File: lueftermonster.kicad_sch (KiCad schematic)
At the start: 87 parts, among them J1 Barrel_Jack, J10 Fan, J11 Fan, J12 Fan, J13 Fan, J14 Fan, J15 Fan, J16 Fan, J17 PROG, J2 Fan, J3 Fan, J4 Fan, J5 Fan, J6 Fan, J7 Fan, J8 Fan, J9 Fan, Q1 Q_PMOS_GSD, Q2 Q_NMOS_GSD, Q3 Q_NMOS_GSD, Q4 Q_NMOS_GSD, Q5 Q_NMOS_GSD, U1 ESP32-WROOM-32E, U2 AOZ1280CI, U3 AMS1117-5.0

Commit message: more bom, all the heavy hitters are in now
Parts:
- C11, C12, C13, C14, C15, C16, C17, C18, C19, C20, C21, C22, C23, C24, C25: LCSC (none) -> C215803; MPN (none) -> FH (Guangdong Fenghua Advanced Tech); Manufacturer (none) -> 0805B105K500NT
- J10, J11, J12, J13, J14, J15, J16, J2, J3, J4, J5, J6, J7, J8, J9: LCSC (none) -> C240840; MPN (none) -> 470531000; Manufacturer (none) -> MOLEX
- R3: LCSC (none) -> C25897; MPN (none) -> 0402WGF4992TCE; Manufacturer (none) -> UNI-ROYAL(Uniroyal Elec)
- R4: LCSC (none) -> C26956; MPN (none) -> 0402WGF1582TCE; Manufacturer (none) -> UNI-ROYAL(Uniroyal Elec)
- R6, R7, R8, R9: LCSC (none) -> C25086; MPN (none) -> 0402WGF100KTCE; Manufacturer (none) -> UNI-ROYAL(Uniroyal Elec)

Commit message: snap
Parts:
- added H1, H2, H3, H4: MountingHole_Pad, MountingHole:MountingHole_3.2mm_M3_ISO14580_Pad, symbol Mechanical:MountingHole_Pad
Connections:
- no-connect marks 8 -> 12

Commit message: use 100mil headers for fans
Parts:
- J10, J11, J12, J13, J14, J15, J16, J2, J3, J4, J5, J6, J7, J8, J9: footprint Connector:FanPinHeader_1x04_P2.54mm_Vertical -> Connector_PinHeader_2.54mm:PinHeader_1x04_P2.54mm_Vertical_SMD_Pin1Right; LCSC C240840 -> C780062; MPN 470531000 -> X6511WVS-04H-C60D48R1; Manufacturer MOLEX -> XKB Connection
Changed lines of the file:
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@@
 			)
 		)
-		(property "Footprint" "Connector:FanPinHeader_1x04_P2.54mm_Vertical"
+		(property "Footprint" "Connector_PinHeader_2.54mm:PinHeader_1x04_P2.54mm_Vertical_SMD_Pin1Right"
 			(at 180.34 88.9 0)
 			(effects
@@
 			)
 		)
-		(property "LCSC" "C240840"
+		(property "LCSC" "C780062"
 			(at 180.34 88.9 0)
 			(effects
@@
 			)
 		)
-		(property "MPN" "470531000"
+		(property "MPN" "X6511WVS-04H-C60D48R1"
 			(at 180.34 88.9 0)
 			(effects
@@
 			)
 		)
-		(property "Manufacturer" "MOLEX"
+		(property "Manufacturer" "XKB Connection"
 			(at 180.34 88.9 0)
 			(effects
@@
 			)
 		)
-		(property "Footprint" "Connector:FanPinHeader_1x04_P2.54mm_Vertical"
+		(property "Footprint" "Connector_PinHeader_2.54mm:PinHeader_1x04_P2.54mm_Vertical_SMD_Pin1Right"
 			(at 209.55 88.9 0)
 			(effects
@@
 			)
 		)
-		(property "LCSC" "C240840"
+		(property "LCSC" "C780062"
 			(at 209.55 88.9 0)
 			(effects
@@
 			)
 		)
-		(property "MPN" "470531000"
+		(property "MPN" "X6511WVS-04H-C60D48R1"
 			(at 209.55 88.9 0)
 			(effects
@@
 			)
 		)
-		(property "Manufacturer" "MOLEX"
+		(property "Manufacturer" "XKB Connection"
 			(at 209.55 88.9 0)
 			(effects
@@
 			)
 		)
-		(property "Footprint" "Connector:FanPinHeader_1x04_P2.54mm_Vertical"
+		(property "Footprint" "Connector_PinHeader_2.54mm:PinHeader_1x04_P2.54mm_Vertical_SMD_Pin1Right"
 			(at 267.97 77.47 0)
 			(effects
@@
 			)
 		)
-		(property "LCSC" "C240840"
+		(property "LCSC" "C780062"
 			(at 267.97 77.47 0)
 			(effects
@@
 			)
 		)
-		(property "MPN" "470531000"
+		(property "MPN" "X6511WVS-04H-C60D48R1"
 			(at 267.97 77.47 0)
 			(effects
@@
 			)
 		)
-		(property "Manufacturer" "MOLEX"
+		(property "Manufacturer" "XKB Connection"
 			(at 267.97 77.47 0)
 			(effects
@@
 			)
 		)
-		(property "Footprint" "Connector:FanPinHeader_1x04_P2.54mm_Vertical"
+		(property "Footprint" "Connector_PinHeader_2.54mm:PinHeader_1x04_P2.54mm_Vertical_SMD_Pin1Right"
 			(at 238.76 66.04 0)
 			(effects
@@
 			)
 		)
-		(property "LCSC" "C240840"
+		(property "LCSC" "C780062"
 			(at 238.76 66.04 0)
 			(effects
@@
 			)
 		)
-		(property "MPN" "470531000"
+		(property "MPN" "X6511WVS-04H-C60D48R1"
 			(at 238.76 66.04 0)
 			(effects
@@
 			)
 		)
-		(property "Manufacturer" "MOLEX"
+		(property "Manufacturer" "XKB Connection"
 			(at 238.76 66.04 0)
 			(effects
@@
 			)
 		)
-		(property "Footprint" "Connector:FanPinHeader_1x04_P2.54mm_Vertical"
+		(property "Footprint" "Connector_PinHeader_2.54mm:PinHeader_1x04_P2.54mm_Vertical_SMD_Pin1Right"
 			(at 238.76 77.47 0)
 			(effects
@@
 			)
 		)
-		(property "LCSC" "C240840"
+		(property "LCSC" "C780062"
 			(at 238.76 77.47 0)
 			(effects
@@
 			)
 		)
-		(property "MPN" "470531000"
+		(property "MPN" "X6511WVS-04H-C60D48R1"
 			(at 238.76 77.47 0)
 			(effects
@@
 			)
 		)
-		(property "Manufacturer" "MOLEX"
+		(property "Manufacturer" "XKB Connection"
 			(at 238.76 77.47 0)
 			(effects
@@
 			)
 		)
-		(property "Footprint" "Connector:FanPinHeader_1x04_P2.54mm_Vertical"
+		(property "Footprint" "Connector_PinHeader_2.54mm:PinHeader_1x04_P2.54mm_Vertical_SMD_Pin1Right"
 			(at 209.55 66.04 0)
 			(effects
@@
 			)
 		)
-		(property "LCSC" "C240840"
+		(property "LCSC" "C780062"
 			(at 209.55 66.04 0)
 			(effects
@@
 			)
 		)
-		(property "MPN" "470531000"
+		(property "MPN" "X6511WVS-04H-C60D48R1"
 			(at 209.55 66.04 0)
 			(effects
@@
 			)
 		)
-		(property "Manufacturer" "MOLEX"
+		(property "Manufacturer" "XKB Connection"
 			(at 209.55 66.04 0)
 			(effects
@@
 			)
 		)
-		(property "Footprint" "Connector:FanPinHeader_1x04_P2.54mm_Vertical"
+		(property "Footprint" "Connector_PinHeader_2.54mm:PinHeader_1x04_P2.54mm_Vertical_SMD_Pin1Right"
 			(at 267.97 66.04 0)
 			(effects
@@
 			)
 		)
-		(property "LCSC" "C240840"
+		(property "LCSC" "C780062"
 			(at 267.97 66.04 0)
 			(effects
@@
 			)
 		)
-		(property "MPN" "470531000"
+		(property "MPN" "X6511WVS-04H-C60D48R1"
 			(at 267.97 66.04 0)
 			(effects
@@
 			)
 		)
-		(property "Manufacturer" "MOLEX"
+		(property "Manufacturer" "XKB Connection"
 			(at 267.97 66.04 0)
 			(effects
@@
 			)
 		)
-		(property "Footprint" "Connector:FanPinHeader_1x04_P2.54mm_Vertical"
+		(property "Footprint" "Connector_PinHeader_2.54mm:PinHeader_1x04_P2.54mm_Vertical_SMD_Pin1Right"
 			(at 180.34 66.04 0)
 			(effects
@@
 			)
 		)
-		(property "LCSC" "C240840"
+		(property "LCSC" "C780062"
 			(at 180.34 66.04 0)
 			(effects
@@
 			)
 		)
-		(property "MPN" "470531000"
+		(property "MPN" "X6511WVS-04H-C60D48R1"
 			(at 180.34 66.04 0)
 			(effects
@@
 			)
 		)
-		(property "Manufacturer" "MOLEX"
+		(property "Manufacturer" "XKB Connection"
 			(at 180.34 66.04 0)
 			(effects
@@
 			)
 		)
-		(property "Footprint" "Connector:FanPinHeader_1x04_P2.54mm_Vertical"
+		(property "Footprint" "Connector_PinHeader_2.54mm:PinHeader_1x04_P2.54mm_Vertical_SMD_Pin1Right"
 			(at 209.55 77.47 0)
 			(effects
@@
 			)
 		)
-		(property "LCSC" "C240840"
+		(property "LCSC" "C780062"
 			(at 209.55 77.47 0)
 			(effects
@@
 			)
 		)
-		(property "MPN" "470531000"
+		(property "MPN" "X6511WVS-04H-C60D48R1"
 			(at 209.55 77.47 0)
 			(effects
@@
 			)
 		)
-		(property "Manufacturer" "MOLEX"
+		(property "Manufacturer" "XKB Connection"
 			(at 209.55 77.47 0)
 			(effects
@@
 			)
 		)
-		(property "Footprint" "Connector:FanPinHeader_1x04_P2.54mm_Vertical"
+		(property "Footprint" "Connector_PinHeader_2.54mm:PinHeader_1x04_P2.54mm_Vertical_SMD_Pin1Right"
 			(at 267.97 88.9 0)
 			(effects
@@
 			)
 		)
-		(property "LCSC" "C240840"
+		(property "LCSC" "C780062"
 			(at 267.97 88.9 0)
 			(effects
@@
 			)
 		)
-		(property "MPN" "470531000"
+		(property "MPN" "X6511WVS-04H-C60D48R1"
 			(at 267.97 88.9 0)
 			(effects
@@
 			)
 		)
-		(property "Manufacturer" "MOLEX"
+		(property "Manufacturer" "XKB Connection"
 			(at 267.97 88.9 0)
 			(effects
@@
 			)
 		)
-		(property "Footprint" "Connector:FanPinHeader_1x04_P2.54mm_Vertical"
+		(property "Footprint" "Connector_PinHeader_2.54mm:PinHeader_1x04_P2.54mm_Vertical_SMD_Pin1Right"
 			(at 238.76 100.33 0)
 			(effects
@@
 			)
 		)
-		(property "LCSC" "C240840"
+		(property "LCSC" "C780062"
 			(at 238.76 100.33 0)
 			(effects
@@
 			)
 		)
-		(property "MPN" "470531000"
+		(property "MPN" "X6511WVS-04H-C60D48R1"
 			(at 238.76 100.33 0)
 			(effects
@@
 			)
 		)
-		(property "Manufacturer" "MOLEX"
+		(property "Manufacturer" "XKB Connection"
 			(at 238.76 100.33 0)
 			(effects
@@
 			)
 		)
-		(property "Footprint" "Connector:FanPinHeader_1x04_P2.54mm_Vertical"
+		(property "Footprint" "Connector_PinHeader_2.54mm:PinHeader_1x04_P2.54mm_Vertical_SMD_Pin1Right"
 			(at 180.34 100.33 0)
 			(effects
@@
 			)
 		)
-		(property "LCSC" "C240840"
+		(property "LCSC" "C780062"
 			(at 180.34 100.33 0)
 			(effects
@@
 			)
 		)
-		(property "MPN" "470531000"
+		(property "MPN" "X6511WVS-04H-C60D48R1"
 			(at 180.34 100.33 0)
 			(effects
@@
 			)
 		)
-		(property "Manufacturer" "MOLEX"
+		(property "Manufacturer" "XKB Connection"
 			(at 180.34 100.33 0)
 			(effects
@@
 			)
 		)
-		(property "Footprint" "Connector:FanPinHeader_1x04_P2.54mm_Vertical"
+		(property "Footprint" "Connector_PinHeader_2.54mm:PinHeader_1x04_P2.54mm_Vertical_SMD_Pin1Right"
 			(at 209.55 100.33 0)
 			(effects
@@
 			)
 		)
-		(property "LCSC" "C240840"
+		(property "LCSC" "C780062"
 			(at 209.55 100.33 0)
 			(effects
@@
 			)
 		)
-		(property "MPN" "470531000"
+		(property "MPN" "X6511WVS-04H-C60D48R1"
 			(at 209.55 100.33 0)
 			(effects
@@
 			)
 		)
-		(property "Manufacturer" "MOLEX"
+		(property "Manufacturer" "XKB Connection"
 			(at 209.55 100.33 0)
 			(effects
@@
 			)
 		)
-		(property "Footprint" "Connector:FanPinHeader_1x04_P2.54mm_Vertical"
+		(property "Footprint" "Connector_PinHeader_2.54mm:PinHeader_1x04_P2.54mm_Vertical_SMD_Pin1Right"
 			(at 238.76 88.9 0)
 			(effects
@@
 			)
 		)
-		(property "LCSC" "C240840"
+		(property "LCSC" "C780062"
 			(at 238.76 88.9 0)
 			(effects
@@
 			)
 		)
-		(property "MPN" "470531000"
+		(property "MPN" "X6511WVS-04H-C60D48R1"
 			(at 238.76 88.9 0)
 			(effects
@@
 			)
 		)
-		(property "Manufacturer" "MOLEX"
+		(property "Manufacturer" "XKB Connection"
 			(at 238.76 88.9 0)
 			(effects
@@
 			)
 		)
-		(property "Footprint" "Connector:FanPinHeader_1x04_P2.54mm_Vertical"
+		(property "Footprint" "Connector_PinHeader_2.54mm:PinHeader_1x04_P2.54mm_Vertical_SMD_Pin1Right"
 			(at 180.34 77.47 0)
 			(effects
@@
 			)
 		)
-		(property "LCSC" "C240840"
+		(property "LCSC" "C780062"
 			(at 180.34 77.47 0)
 			(effects
@@
 			)
 		)
-		(property "MPN" "470531000"
+		(property "MPN" "X6511WVS-04H-C60D48R1"
 			(at 180.34 77.47 0)
 			(effects
@@
 			)
 		)
-		(property "Manufacturer" "MOLEX"
+		(property "Manufacturer" "XKB Connection"
 			(at 180.34 77.47 0)
 			(effects

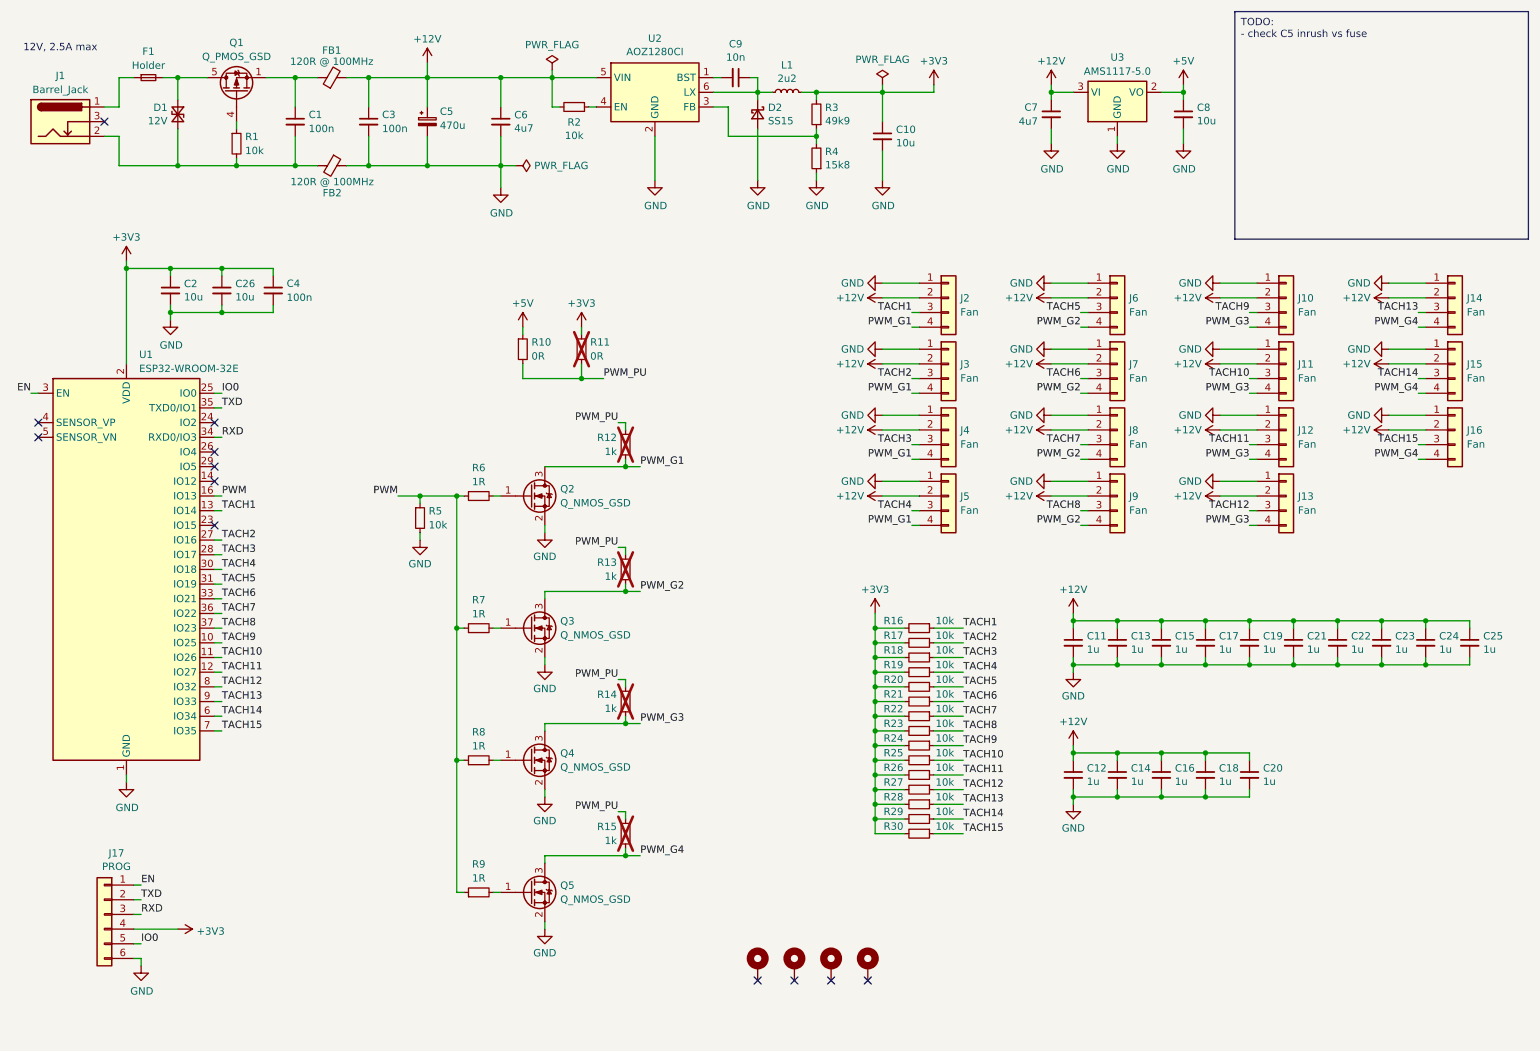
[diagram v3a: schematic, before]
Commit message: finalize bom, add LED
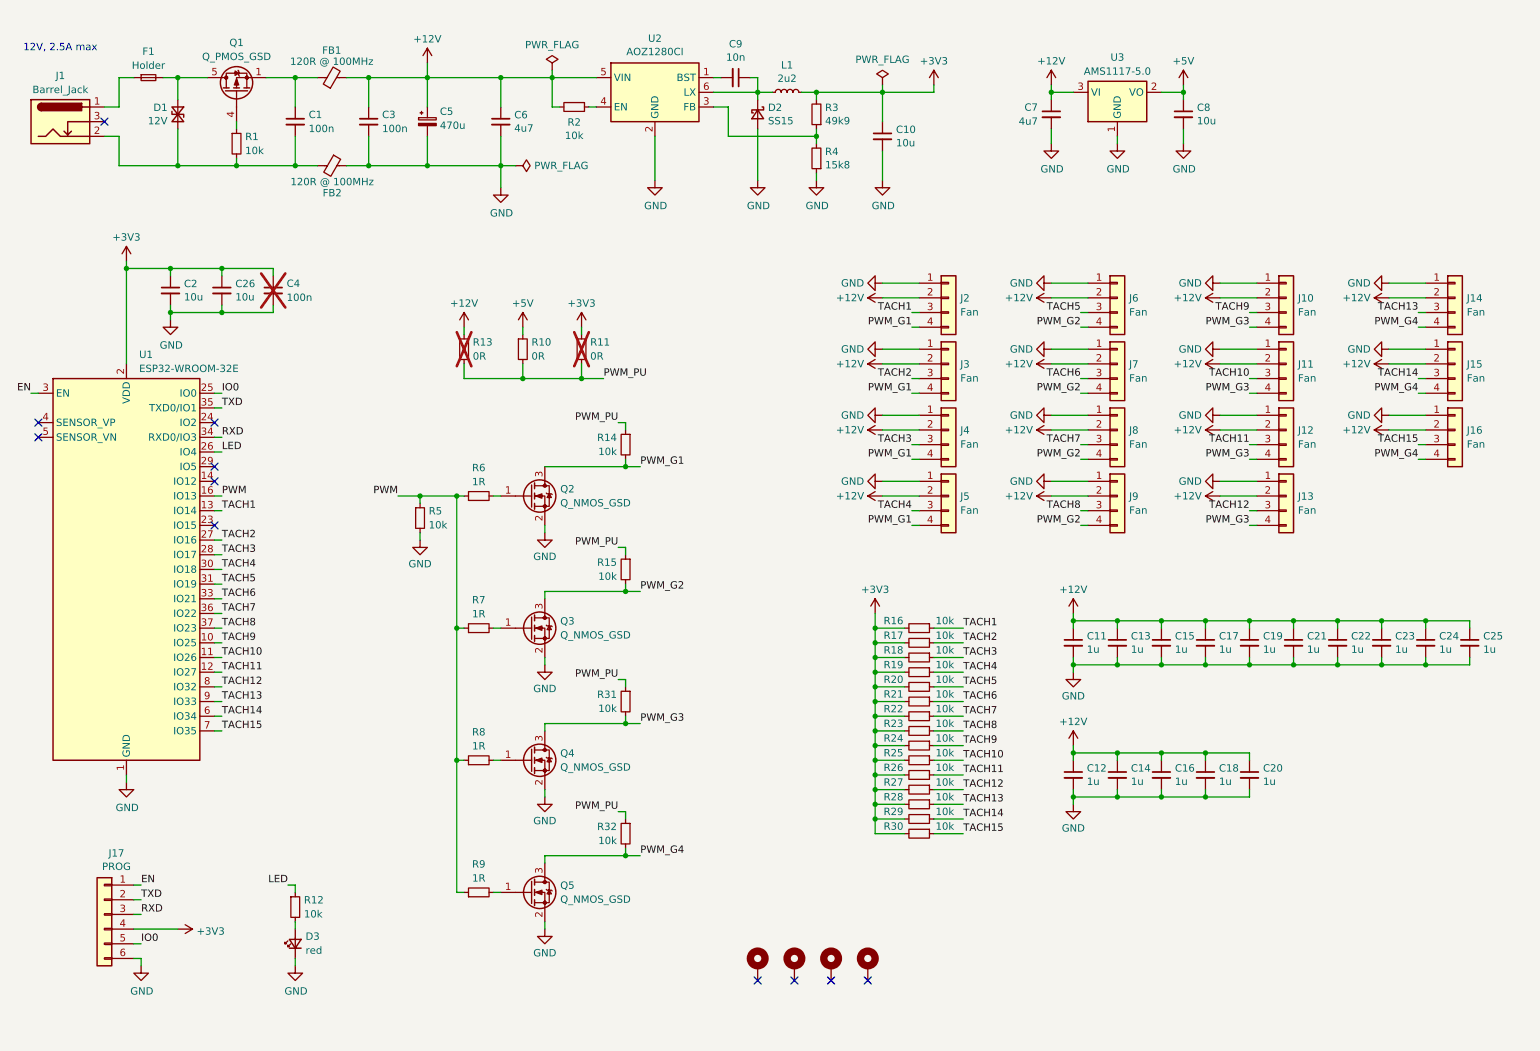
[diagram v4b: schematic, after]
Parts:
- added D3: red, LED_SMD:LED_0603_1608Metric, symbol Device:LED_Small
- added R31, R32: 10k, Resistor_SMD:R_0402_1005Metric, symbol Device:R_Small
- C1, C3: MPN (none) -> CL21B104KCFNNNE; Manufacturer (none) -> Samsung Electro-Mechanics
- C11, C12, C13, C14, C15, C16, C17, C18, C19, C20, C21, C22, C23, C24, C25: MPN FH (Guangdong Fenghua Advanced Tech) -> 0805B105K500NT; Manufacturer 0805B105K500NT -> FH (Guangdong Fenghua Advanced Tech)
- C4: now not fitted
- C9: LCSC (none) -> C15195; MPN (none) -> CL05B103KB5NNNC; Manufacturer (none) -> Samsung Electro-Mechanics
- J17: LCSC (none) -> C2883763; MPN (none) -> X6511WVS-06H-C60D48R2; Manufacturer (none) -> XKB Connection
- R12, R14, R15: value 1k -> 10k; footprint Resistor_SMD:R_0603_1608Metric_Pad0.98x0.95mm_HandSolder -> Resistor_SMD:R_0402_1005Metric; LCSC C11702 -> C25744; MPN 0402WGF1001TCE -> 0402WGF1002TCE; now fitted
- R13: value 1k -> 0R; LCSC C11702 -> C21189; MPN 0402WGF1001TCE -> 0603WAF0000T5E
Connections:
- net +12V: now also R13.1
- net GND: now also D3.1 (K)
- net PWM_G1: now also R14.2; no longer R12.2
- net PWM_G2: now also R15.2; no longer R13.2
- net PWM_G3: now also R31.2; no longer R14.2
- net PWM_G4: now also R32.2; no longer R15.2
- net PWM_PU: now also R13.2, R31.1, R32.1; no longer R12.1, R13.1
- net LED: now reaches U1.26 (IO4)
- net LED: now also R12.1
- new net: D3.2 (A), R12.2
- no-connect marks 12 -> 11

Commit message: snap
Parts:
- removed C26: 10u, Capacitor_SMD:C_0805_2012Metric, symbol Device:C_Small
- removed C4: 100n, Capacitor_SMD:C_0402_1005Metric, symbol Device:C_Small
- removed D3: red, LED_SMD:LED_0603_1608Metric, symbol Device:LED_Small
- removed Q5: Q_NMOS_GSD, Package_TO_SOT_SMD:SOT-23, symbol Device:Q_NMOS_GSD
- added C?: 10n, Capacitor_SMD:C_0402_1005Metric, symbol Device:C_Small
- added J18, J19, J20, J21: W1, Connector_PinHeader_2.54mm:PinHeader_1x03_P2.54mm_Vertical_SMD_Pin1Left, symbol Connector_Generic:Conn_01x03
- added R?: 10k, Resistor_SMD:R_0402_1005Metric, symbol Device:R_Small
- L1: footprint Inductor_SMD:L_Taiyo-Yuden_NR-24xx -> Inductor_SMD:L_1008_2520Metric; Digikey 587-3443-1-ND -> (none); LCSC (none) -> C576403; MPN NRH2412T2R2MNGH -> DFE252012F-2R2M=P2; Manufacturer Taiyo Yuden -> Murata Electronics
- R12: value 10k -> 0R; footprint Resistor_SMD:R_0402_1005Metric -> Resistor_SMD:R_0603_1608Metric_Pad0.98x0.95mm_HandSolder; LCSC C25744 -> C21189; MPN 0402WGF1002TCE -> 0603WAF0000T5E; now not fitted
- R32: value 10k -> 0R; footprint Resistor_SMD:R_0402_1005Metric -> Resistor_SMD:R_0603_1608Metric_Pad0.98x0.95mm_HandSolder; LCSC C25744 -> C21189; MPN 0402WGF1002TCE -> 0603WAF0000T5E
- R9: value 1R -> TBD; LCSC C25086 -> (none); MPN 0402WGF100KTCE -> (none); Manufacturer UNI-ROYAL(Uniroyal Elec) -> (none)
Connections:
- net +3V3: now also R32.1, R9.1, R?.1
- net +5V: now also R12.1
- net EN: now also C?.1, R?.2
- net GND: now also C?.2, J18.3 (Pin_3), J19.3 (Pin_3), J20.3 (Pin_3), J21.3 (Pin_3)
- net PWM: no longer R9.1
- net PWM_G1: now also J14.4 (Pin_4)
- net PWM_G2: now also J15.4 (Pin_4)
- net PWM_G3: now also J16.4 (Pin_4)
- net PWM_PU: no longer R32.1
- net TACH1: now also U1.37 (IO23); no longer U1.13 (IO14)
- net TACH10: now also J15.3 (Pin_3), U1.8 (IO32); no longer J11.3 (Pin_3), U1.11 (IO26)
- net TACH11: now also J10.3 (Pin_3), U1.9 (IO33); no longer J12.3 (Pin_3), U1.12 (IO27)
- net TACH12: now also J11.3 (Pin_3), U1.10 (IO25); no longer J13.3 (Pin_3), U1.8 (IO32)
- net TACH13: now also J12.3 (Pin_3), U1.11 (IO26); no longer J14.3 (Pin_3), U1.9 (IO33)
- net TACH14: now also J13.3 (Pin_3), U1.12 (IO27); no longer J15.3 (Pin_3), U1.6 (IO34)
- net TACH15: now also U1.13 (IO14); no longer U1.7 (IO35)
- net TACH2: now also U1.36 (IO22); no longer U1.27 (IO16)
- net TACH3: now also U1.33 (IO21); no longer U1.28 (IO17)
- net TACH4: now also U1.31 (IO19); no longer U1.30 (IO18)
- net TACH5: now also J14.3 (Pin_3), U1.30 (IO18); no longer J6.3 (Pin_3), U1.31 (IO19)
- net TACH6: now also J6.3 (Pin_3), U1.28 (IO17); no longer J7.3 (Pin_3), U1.33 (IO21)
- net TACH7: now also J7.3 (Pin_3), U1.27 (IO16); no longer J8.3 (Pin_3), U1.36 (IO22)
- net TACH8: now also J8.3 (Pin_3), U1.6 (IO34); no longer J9.3 (Pin_3), U1.37 (IO23)
- net TACH9: now also J9.3 (Pin_3), U1.7 (IO35); no longer J10.3 (Pin_3), U1.10 (IO25)
- net W1_SUPPLY: now reaches R12.2
- net W1_SUPPLY: now also R32.2, J18.1 (Pin_1), J19.1 (Pin_1), J20.1 (Pin_1), J21.1 (Pin_1)
- net W1: now reaches R9.2
- net W1: now also U1.26 (IO4), J18.2 (Pin_2), J19.2 (Pin_2), J20.2 (Pin_2), J21.2 (Pin_2)
- removed net LED: R12.1, U1.26 (IO4)
- removed net PWM_G4: J14.4 (Pin_4), J15.4 (Pin_4), J16.4 (Pin_4), R32.2
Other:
- moved on the sheet: C2, J10, J11, J12, J13, J14, J15, J16, J2, J3, J4, J5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
